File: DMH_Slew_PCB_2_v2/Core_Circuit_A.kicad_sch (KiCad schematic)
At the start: 52 parts, among them J1 TS_Jack_6.35mm_Sw, J2 TS_Jack_6.35mm_Sw, J3 TS_Jack_6.35mm_Sw, J50 Conn_01x08_PinHeader, J51 Conn_01x08_PinHeader, Q1 BC548, Q2 BC548, Q3 BC558, Q4 BC558, SW1 SW_DPDT_3way, SW2 SW_DPDT, SW3 SPDT_OnOffOn, U1 TL074, U2 TL074

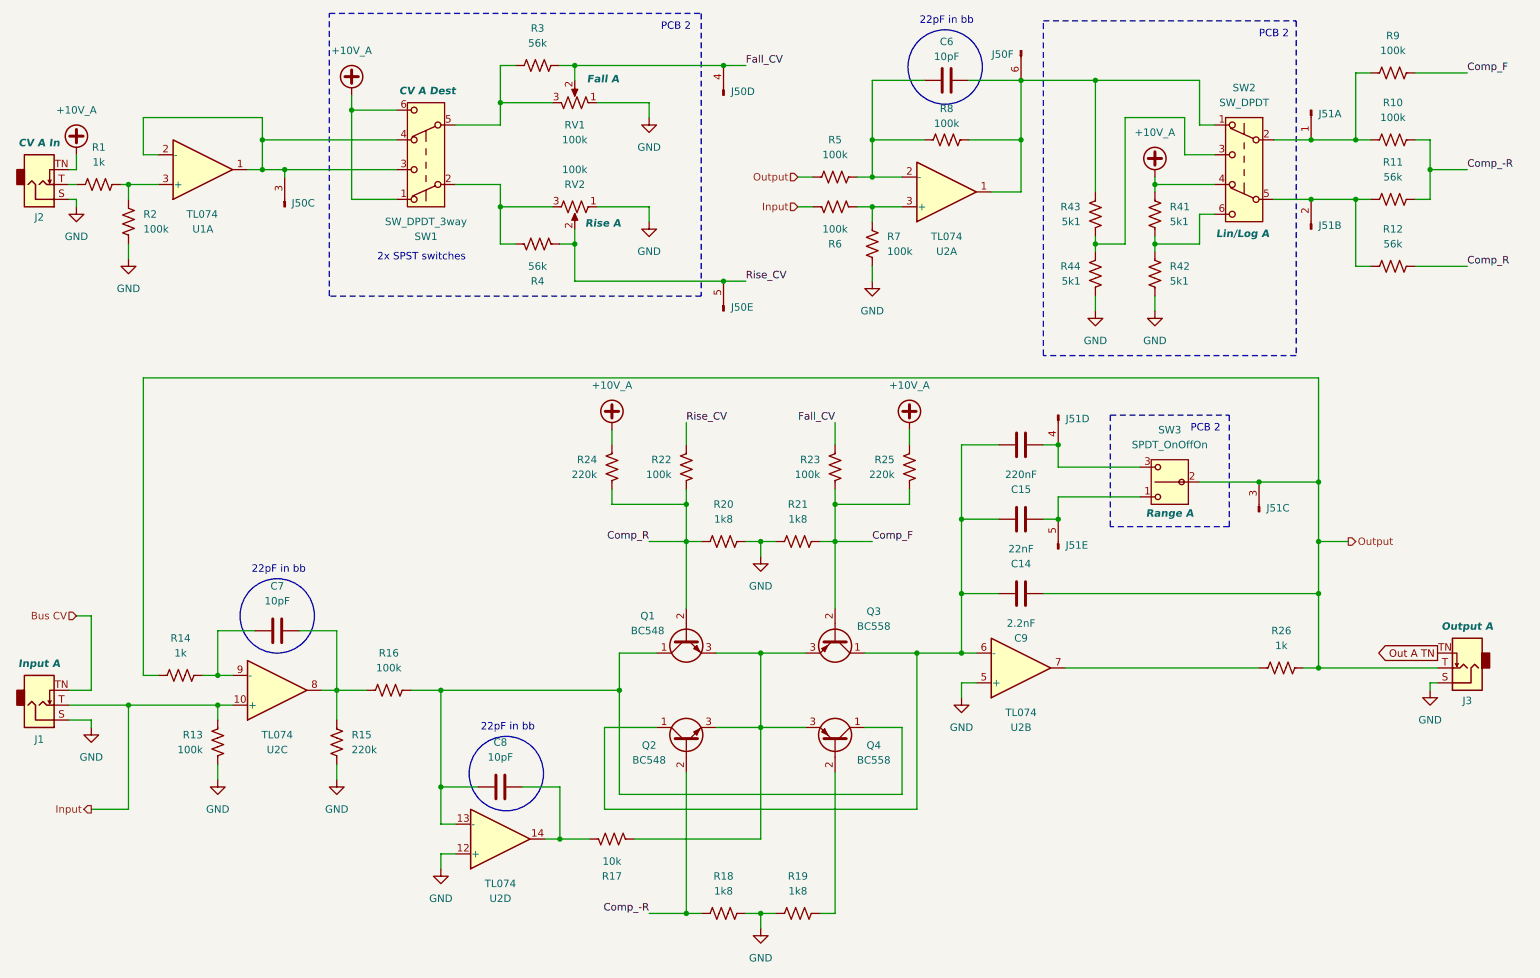
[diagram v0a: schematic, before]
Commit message: PCB 2 component placement done
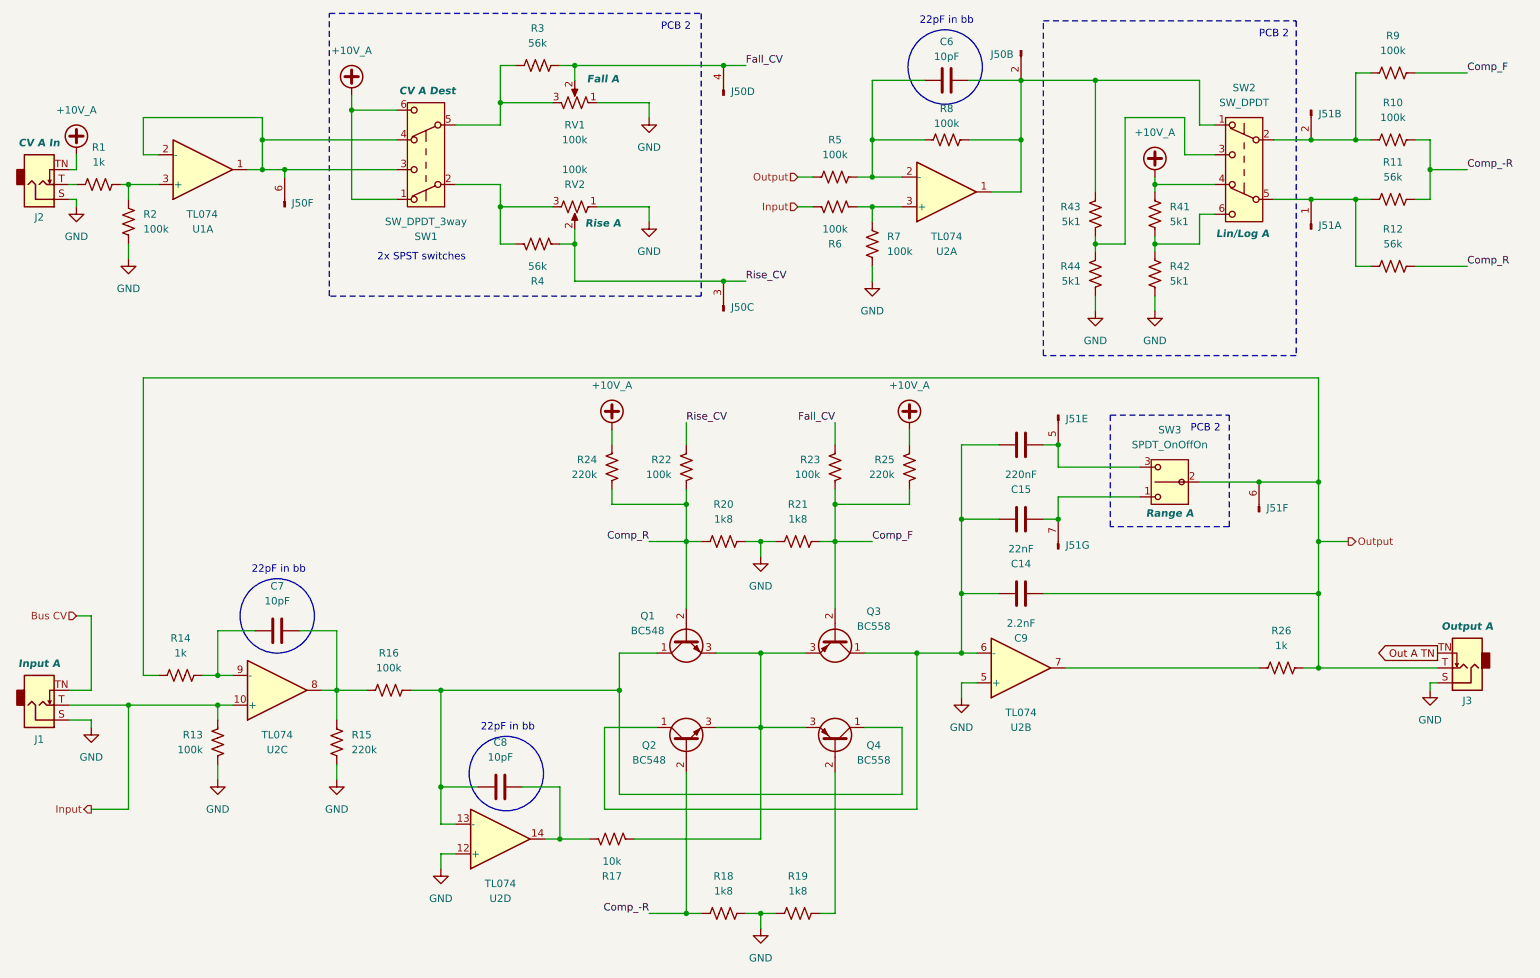
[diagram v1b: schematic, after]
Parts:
- J50, J51: footprint Connector_PinHeader_2.54mm:PinHeader_1x08_P2.54mm_Vertical -> Connector_PinSocket_2.54mm:PinSocket_1x08_P2.54mm_Vertical
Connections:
- net Output: now also J51.6 (Pin_6); no longer J51.3 (Pin_3)
- net Rise_CV: now also J50.3 (Pin_3); no longer J50.5 (Pin_5)
- net at C6.2, R43.1, R8.1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: now also J50.2 (Pin_2); no longer J50.6 (Pin_6)
- net at C15.2, SW3.3 (C): now also J51.5 (Pin_5); no longer J51.4 (Pin_4)
- net at R11.2, R12.2, SW2.5 (B): now also J51.1 (Pin_1); no longer J51.2 (Pin_2)
- net at SW1.3 (C), SW1.4 (A), U1.1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: now also J50.6 (Pin_6); no longer J50.3 (Pin_3)
- net at R10.2, R9.2, SW2.2 (B): now also J51.2 (Pin_2); no longer J51.1 (Pin_1)
- net at C14.2, SW3.1 (A): now also J51.7 (Pin_7); no longer J51.5 (Pin_5)
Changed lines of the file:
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@@
 		(at 190.5 30.48 90)
 		(mirror x)
-		(unit 6)
+		(unit 2)
 		(exclude_from_sim no)
 		(in_bom yes)
@@
 			)
 		)
-		(property "Footprint" "Connector_PinHeader_2.54mm:PinHeader_1x08_P2.54mm_Vertical"
+		(property "Footprint" "Connector_PinSocket_2.54mm:PinSocket_1x08_P2.54mm_Vertical"
 			(at 190.5 30.48 0)
 			(effects
@@
 				(path "/58f4306d-5387-4983-bb08-41a2313fd315/7ad2d702-dfb7-4d49-a82d-34430dd5948f"
 					(reference "J50")
-					(unit 6)
+					(unit 2)
 				)
 			)
@@
 			)
 		)
-		(property "Footprint" "Connector_PinHeader_2.54mm:PinHeader_1x08_P2.54mm_Vertical"
+		(property "Footprint" "Connector_PinSocket_2.54mm:PinSocket_1x08_P2.54mm_Vertical"
 			(at 139.7 38.1 0)
 			(effects
@@
 		(lib_id "SynthStuff:Conn_01x08_PinHeader")
 		(at 240.03 60.96 90)
-		(unit 2)
+		(unit 1)
 		(exclude_from_sim no)
 		(in_bom yes)
@@
 			)
 		)
-		(property "Footprint" "Connector_PinHeader_2.54mm:PinHeader_1x08_P2.54mm_Vertical"
+		(property "Footprint" "Connector_PinSocket_2.54mm:PinSocket_1x08_P2.54mm_Vertical"
 			(at 240.03 60.96 0)
 			(effects
@@
 				(path "/58f4306d-5387-4983-bb08-41a2313fd315/7ad2d702-dfb7-4d49-a82d-34430dd5948f"
 					(reference "J51")
-					(unit 2)
+					(unit 1)
 				)
 			)
@@
 		(lib_id "SynthStuff:Conn_01x08_PinHeader")
 		(at 231.14 109.22 90)
-		(unit 3)
+		(unit 6)
 		(exclude_from_sim no)
 		(in_bom yes)
@@
 			)
 		)
-		(property "Footprint" "Connector_PinHeader_2.54mm:PinHeader_1x08_P2.54mm_Vertical"
+		(property "Footprint" "Connector_PinSocket_2.54mm:PinSocket_1x08_P2.54mm_Vertical"
 			(at 231.14 109.22 0)
 			(effects
@@
 				(path "/58f4306d-5387-4983-bb08-41a2313fd315/7ad2d702-dfb7-4d49-a82d-34430dd5948f"
 					(reference "J51")
-					(unit 3)
+					(unit 6)
 				)
 			)
@@
 		(lib_id "SynthStuff:Conn_01x08_PinHeader")
 		(at 196.85 115.57 90)
-		(unit 5)
+		(unit 7)
 		(exclude_from_sim no)
 		(in_bom yes)
@@
 			)
 		)
-		(property "Footprint" "Connector_PinHeader_2.54mm:PinHeader_1x08_P2.54mm_Vertical"
+		(property "Footprint" "Connector_PinSocket_2.54mm:PinSocket_1x08_P2.54mm_Vertical"
 			(at 196.85 115.57 0)
 			(effects
@@
 				(path "/58f4306d-5387-4983-bb08-41a2313fd315/7ad2d702-dfb7-4d49-a82d-34430dd5948f"
 					(reference "J51")
-					(unit 5)
+					(unit 7)
 				)
 			)
@@
 		(lib_id "SynthStuff:Conn_01x08_PinHeader")
 		(at 64.77 57.15 90)
-		(unit 3)
+		(unit 6)
 		(exclude_from_sim no)
 		(in_bom yes)
@@
 			)
 		)
-		(property "Footprint" "Connector_PinHeader_2.54mm:PinHeader_1x08_P2.54mm_Vertical"
+		(property "Footprint" "Connector_PinSocket_2.54mm:PinSocket_1x08_P2.54mm_Vertical"
 			(at 64.77 57.15 0)
 			(effects
@@
 				(path "/58f4306d-5387-4983-bb08-41a2313fd315/7ad2d702-dfb7-4d49-a82d-34430dd5948f"
 					(reference "J50")
-					(unit 3)
+					(unit 6)
 				)
 			)
@@
 		(lib_id "SynthStuff:Conn_01x08_PinHeader")
 		(at 196.85 92.71 270)
-		(unit 4)
+		(unit 5)
 		(exclude_from_sim no)
 		(in_bom yes)
@@
 			)
 		)
-		(property "Footprint" "Connector_PinHeader_2.54mm:PinHeader_1x08_P2.54mm_Vertical"
+		(property "Footprint" "Connector_PinSocket_2.54mm:PinSocket_1x08_P2.54mm_Vertical"
 			(at 196.85 92.71 0)
 			(effects
@@
 				(path "/58f4306d-5387-4983-bb08-41a2313fd315/7ad2d702-dfb7-4d49-a82d-34430dd5948f"
 					(reference "J51")
-					(unit 4)
+					(unit 5)
 				)
 			)
@@
 		(lib_id "SynthStuff:Conn_01x08_PinHeader")
 		(at 240.03 40.64 270)
-		(unit 1)
+		(unit 2)
 		(exclude_from_sim no)
 		(in_bom yes)
@@
 			)
 		)
-		(property "Footprint" "Connector_PinHeader_2.54mm:PinHeader_1x08_P2.54mm_Vertical"
+		(property "Footprint" "Connector_PinSocket_2.54mm:PinSocket_1x08_P2.54mm_Vertical"
 			(at 240.03 40.64 0)
 			(effects
@@
 				(path "/58f4306d-5387-4983-bb08-41a2313fd315/7ad2d702-dfb7-4d49-a82d-34430dd5948f"
 					(reference "J51")
-					(unit 1)
+					(unit 2)
 				)
 			)
@@
 		(lib_id "SynthStuff:Conn_01x08_PinHeader")
 		(at 139.7 74.93 90)
-		(unit 5)
+		(unit 3)
 		(exclude_from_sim no)
 		(in_bom yes)
@@
 			)
 		)
-		(property "Footprint" "Connector_PinHeader_2.54mm:PinHeader_1x08_P2.54mm_Vertical"
+		(property "Footprint" "Connector_PinSocket_2.54mm:PinSocket_1x08_P2.54mm_Vertical"
 			(at 139.7 74.93 0)
 			(effects
@@
 				(path "/58f4306d-5387-4983-bb08-41a2313fd315/7ad2d702-dfb7-4d49-a82d-34430dd5948f"
 					(reference "J50")
-					(unit 5)
+					(unit 3)
 				)
 			)

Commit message: Updated Log circuit
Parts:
- removed R41, R42, R43, R44: 5k1, Resistor_THT:R_Axial_DIN0207_L6.3mm_D2.5mm_P7.62mm_Horizontal, symbol Device:R_US
- R11, R12: value 56k -> 100k
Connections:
- net GND: now also SW2.3 (C), SW2.6 (C)
